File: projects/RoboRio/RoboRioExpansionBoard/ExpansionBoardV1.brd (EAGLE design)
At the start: 96.2 x 80 mm, 92 parts, among them J1 RRINTERFACE-FEMALE, J2 MICROSD, Q1 5MHz, U1 P8X32A-D40, U2 24LC256P, U3 BUTTON, U4 MCP3008, U5 MC1525TO

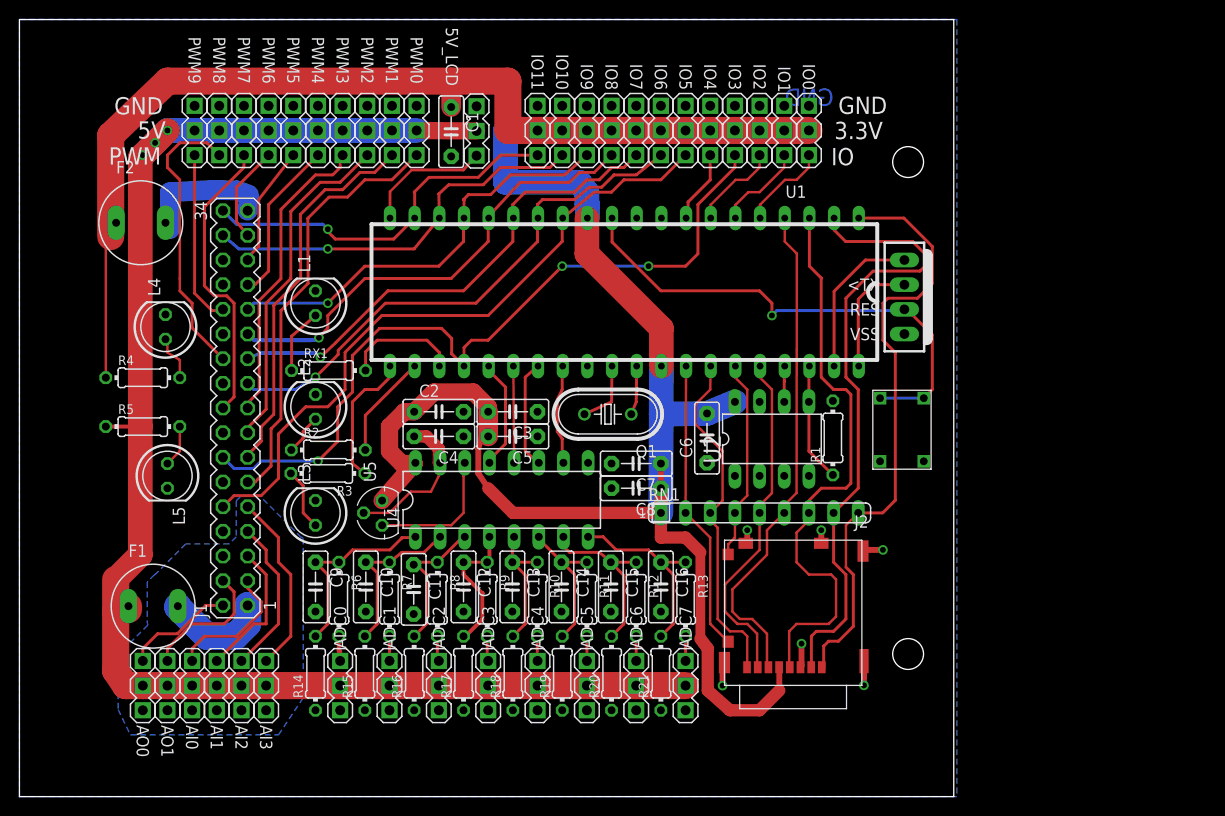
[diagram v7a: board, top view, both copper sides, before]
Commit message: Finished silkscreen labels
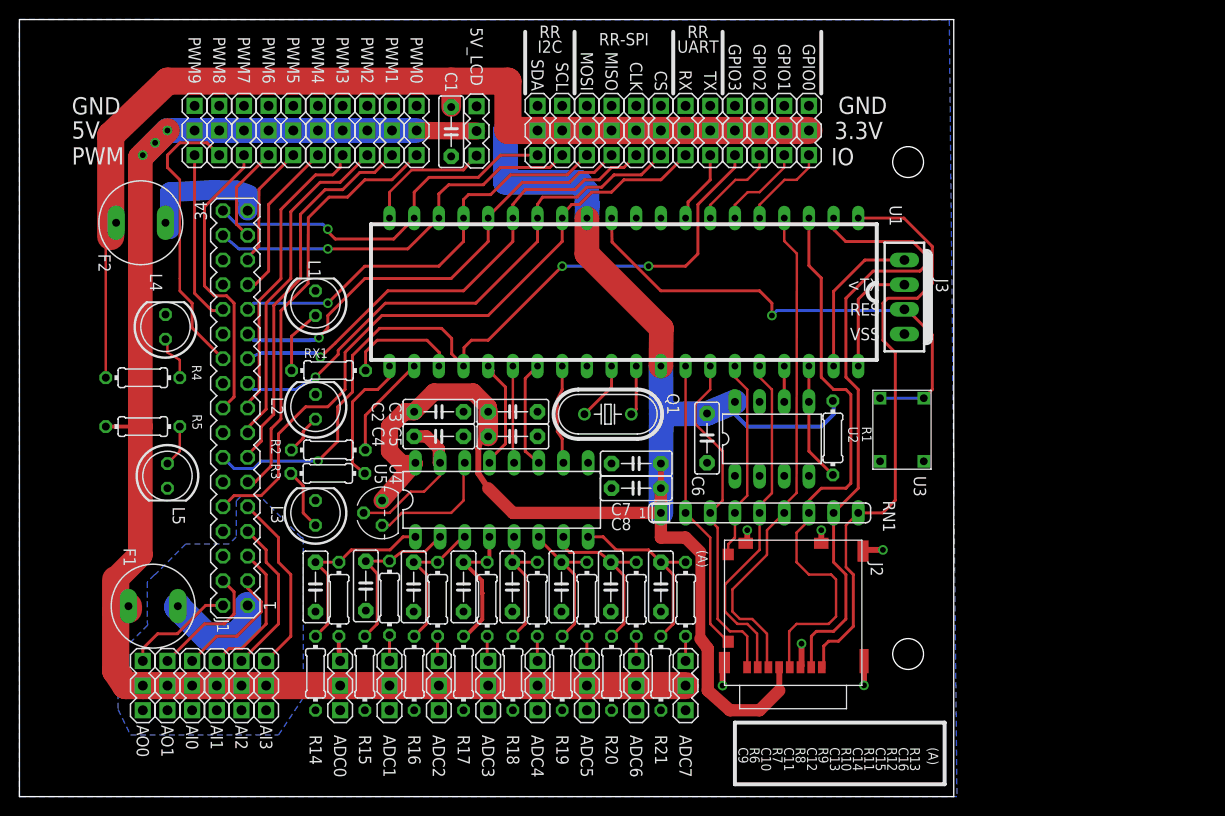
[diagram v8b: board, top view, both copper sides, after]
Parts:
- moved C11 0.25 mm to (45.7, 21.6)
- moved R7 0.13 mm to (43.2, 20.4)
- moved C10 0.10 mm to (40.7, 21.7)
- moved U1 0.05 mm to (67.9, 51.9)
- renumbered U$3 to J3
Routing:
- net +3V3: track 295.8 -> 309.8 mm
- net AO1: track 13.5 -> 12.8 mm
- net AI0: track 13.7 -> 13.0 mm
- net N$16: track 15.3 -> 16.0 mm
- net DGND: track 26.7 -> 26.0 mm
- net N$2: track 6.75 -> 6.11 mm
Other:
- board text added: "(A)"
- board text added: "CLK"
- board text added: "CS"
- board text added: "GPIO0 GPIO1 GPIO2 GPIO3"
- board text added: "J3"
- board text added: "MISO"
- board text added: "MOSI"
- board text added: "R13 C16 R12 C15 R11 C14 R10 C13 R9 C12 R8 C11 R7 C10 R6 C9"
- board text added: "RR I2C"
- board text added: "RR UART"
- board text added: "RR-SPI"
- board text added: "RX"
- board text added: "SCL"
- board text added: "SDA"
- board text added: "TX"
- board text added: "U3"
